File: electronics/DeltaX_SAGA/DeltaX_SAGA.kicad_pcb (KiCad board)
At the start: 4 copper layers, 50 x 50 mm, 73 parts, among them J1 USB_B_Micro, J10 M3_Encoder, J11 M12, J12 M21, J13 M22, J14 M31, J15 M33, J16 Thrower+, J17 Thrower-, J2 Programmer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

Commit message: PCB design updated
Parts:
- J11: value M12 -> OUT-
- J12: value M21 -> OUT+
- J13: value M22 -> OUT-
- J14: value M31 -> OUT+
- J15: value M33 -> OUT-
- J16: value Thrower+ -> THRWR+
- J17: value Thrower- -> THRWR-
- J4: value M11 -> OUT+
- J5: value Battery+ -> BAT+
- J7: value Battery- -> BAT-
- moved J4 0.58 mm to (135.8, 85.2)
- moved J16 0.50 mm to (172.4, 102.3)
- moved J17 0.50 mm to (172.4, 99.0)
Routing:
- net +3.3V: track 16.3 -> 16.7 mm, vias 11 -> 10
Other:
- board text added: "+"
- board text added: "-"
- board text added: "S"

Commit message: PCB dsign updated
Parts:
- moved Q1 4.78 mm to (164.0, 98.7)
- moved R3 4.34 mm to (158.7, 100.2), turned to 180 degrees
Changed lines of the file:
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@@
   )
   (footprint "Resistor_SMD:R_0603_1608Metric" (layer "B.Cu")
-    (at 154.3304 99.8728 90)
+    (at 158.66 100.15 180)
     (descr "Resistor SMD 0603 (1608 Metric), square (rectangular) end terminal, IPC_7351 nominal, (Body size source: IPC-SM-782 page 72, https://www.pcb-3d.com/wordpress/wp-content/uploads/ipc-sm-782a_amendment_1_and_2.pdf), generated with kicad-footprint-generator")
     (tags "resistor")
@@
     (property "Sheetname" "")
     (attr smd)
-    (fp_text reference "R3" (at -2.2972 -0.0704) (layer "B.SilkS")
-      (effects (font (size 1 1) (thickness 0.2)) (justify mirror))
-    )
-    (fp_text value "100" (at 0.9398 -1.1176 90) (layer "B.Fab")
+    (fp_text reference "R3" (at 0.91 1.46 180) (layer "B.SilkS")
+      (effects (font (size 1 1) (thickness 0.2)) (justify mirror))
+    )
+    (fp_text value "100" (at 0.9398 -1.1176) (layer "B.Fab")
       (effects (font (size 0.4 0.4) (thickness 0.1)) (justify mirror))
     )
-    (fp_text user "${REFERENCE}" (at 0 0 90) (layer "B.Fab")
+    (fp_text user "${REFERENCE}" (at 0 0) (layer "B.Fab")
       (effects (font (size 0.4 0.4) (thickness 0.06)) (justify mirror))
     )
@@
     (fp_line (start -0.8 0.4125) (end 0.8 0.4125) (layer "B.Fab") (width 0.1))
     (fp_line (start -0.8 -0.4125) (end -0.8 0.4125) (layer "B.Fab") (width 0.1))
-    (pad "1" smd roundrect (at -0.825 0 90) (size 0.8 0.95) (layers "B.Cu" "B.Paste" "B.Mask") (roundrect_rratio 0.25)
+    (pad "1" smd roundrect (at -0.825 0 180) (size 0.8 0.95) (layers "B.Cu" "B.Paste" "B.Mask") (roundrect_rratio 0.25)
       (net 83 "Net-(Q1-Pad4)") (pintype "passive"))
-    (pad "2" smd roundrect (at 0.825 0 90) (size 0.8 0.95) (layers "B.Cu" "B.Paste" "B.Mask") (roundrect_rratio 0.25)
+    (pad "2" smd roundrect (at 0.825 0 180) (size 0.8 0.95) (layers "B.Cu" "B.Paste" "B.Mask") (roundrect_rratio 0.25)
       (net 5 "GND2") (pintype "passive"))
     (model "${KICAD6_3DMODEL_DIR}/Resistor_SMD.3dshapes/R_0603_1608Metric.wrl"
@@
   )
   (footprint "BUK6Y10:TO127P600X120-5N" (layer "B.Cu")
-    (at 159.2114 99.21745 90)
+    (at 163.9664 98.72645 90)
     (property "MANUFACTURER" "")
     (property "MAXIMUM_PACKAGE_HEIGHT" "")
@@
   (segment (start 145.923 115.5192) (end 150.612695 115.5192) (width 0.25) (layer "B.Cu") (net 3))
   (segment (start 154.219495 119.126) (end 154.6606 119.126) (width 0.25) (layer "B.Cu") (net 3))
-  (via (at 158.5214 99.3902) (size 0.45) (drill 0.2) (layers "F.Cu" "B.Cu") (net 4))
-  (via (at 161.9504 97.9678) (size 0.45) (drill 0.2) (layers "F.Cu" "B.Cu") (net 4))
-  (via (at 160.0962 100.711) (size 0.45) (drill 0.2) (layers "F.Cu" "B.Cu") (net 4))
-  (via (at 158.496 100.711) (size 0.45) (drill 0.2) (layers "F.Cu" "B.Cu") (net 4))
-  (via (at 158.5214 97.9678) (size 0.45) (drill 0.2) (layers "F.Cu" "B.Cu") (net 4))
-  (via (at 161.9504 99.3902) (size 0.45) (drill 0.2) (layers "F.Cu" "B.Cu") (net 4))
-  (via (at 161.925 100.711) (size 0.45) (drill 0.2) (layers "F.Cu" "B.Cu") (net 4))
-  (via (at 160.1216 97.9678) (size 0.45) (drill 0.2) (layers "F.Cu" "B.Cu") (net 4))
-  (via (at 160.1216 99.3902) (size 0.45) (drill 0.2) (layers "F.Cu" "B.Cu") (net 4))
-  (via (at 161.9504 96.6724) (size 0.45) (drill 0.2) (layers "F.Cu" "B.Cu") (net 4))
-  (via (at 158.5214 96.6724) (size 0.45) (drill 0.2) (layers "F.Cu" "B.Cu") (net 4))
-  (via (at 160.1216 96.6724) (size 0.45) (drill 0.2) (layers "F.Cu" "B.Cu") (net 4))
+  (via (at 163.2764 98.8992) (size 0.45) (drill 0.2) (layers "F.Cu" "B.Cu") (net 4))
+  (via (at 166.7054 97.4768) (size 0.45) (drill 0.2) (layers "F.Cu" "B.Cu") (net 4))
+  (via (at 164.8512 100.22) (size 0.45) (drill 0.2) (layers "F.Cu" "B.Cu") (net 4))
+  (via (at 163.251 100.22) (size 0.45) (drill 0.2) (layers "F.Cu" "B.Cu") (net 4))
+  (via (at 163.2764 97.4768) (size 0.45) (drill 0.2) (layers "F.Cu" "B.Cu") (net 4))
+  (via (at 166.7054 98.8992) (size 0.45) (drill 0.2) (layers "F.Cu" "B.Cu") (net 4))
+  (via (at 166.68 100.22) (size 0.45) (drill 0.2) (layers "F.Cu" "B.Cu") (net 4))
+  (via (at 164.8766 97.4768) (size 0.45) (drill 0.2) (layers "F.Cu" "B.Cu") (net 4))
+  (via (at 164.8766 98.8992) (size 0.45) (drill 0.2) (layers "F.Cu" "B.Cu") (net 4))
+  (via (at 166.7054 96.1814) (size 0.45) (drill 0.2) (layers "F.Cu" "B.Cu") (net 4))
+  (via (at 163.2764 96.1814) (size 0.45) (drill 0.2) (layers "F.Cu" "B.Cu") (net 4))
+  (via (at 164.8766 96.1814) (size 0.45) (drill 0.2) (layers "F.Cu" "B.Cu") (net 4))
   (segment (start 138.2776 92.075) (end 138.596401 92.393801) (width 0.25) (layer "F.Cu") (net 5))
   (segment (start 134.734 104.5334) (end 134.9248 104.7242) (width 0.25) (layer "F.Cu") (net 5))
@@
   (via (at 172.4146 100.0086) (size 0.45) (drill 0.2) (layers "F.Cu" "B.Cu") (net 5))
   (via (at 138.2454 95.1) (size 0.45) (drill 0.2) (layers "F.Cu" "B.Cu") (net 5))
-  (via (at 154.051 98.8822) (size 0.45) (drill 0.2) (layers "F.Cu" "B.Cu") (net 5))
+  (via (at 157.62 100.42) (size 0.45) (drill 0.2) (layers "F.Cu" "B.Cu") (net 5))
   (via (at 172.339 95.4278) (size 0.45) (drill 0.2) (layers "F.Cu" "B.Cu") (net 5))
   (via (at 147.701 103.7082) (size 0.45) (drill 0.2) (layers "F.Cu" "B.Cu") (net 5))
@@
   (segment (start 162.1876 120.3008) (end 162.3516 120.1368) (width 0.153162) (layer "F.Cu") (net 7))
   (segment (start 167.061 120.1368) (end 170.7694 120.1368) (width 0.153162) (layer "F.Cu") (net 7))
-  (segment (start 165.8862 119.7368) (end 166.4868 119.1362) (width 0.153162) (layer "F.Cu") (net 8))
-  (segment (start 171.6706 119.634) (end 170.8682 119.634) (width 0.153162) (layer "F.Cu") (net 8))
-  (segment (start 162.358 119.7368) (end 165.8862 119.7368) (width 0.153162) (layer "F.Cu") (net 8))
-  (segment (start 162.122 119.5008) (end 162.358 119.7368) (width 0.153162) (layer "F.Cu") (net 8))
+  (segment (start 170.8682 119.634) (end 171.6706 119.634) (width 0.153162) (layer "F.Cu") (net 8))
+  (segment (start 162.404838 119.783638) (end 165.839362 119.783638) (width 0.153162) (layer "F.Cu") (net 8))
+  (segment (start 167.129238 119.783638) (end 170.718562 119.783638) (width 0.153162) (layer "F.Cu") (net 8))
+  (segment (start 161.1266 119.5008) (end 162.122 119.5008) (width 0.153162) (layer "F.Cu") (net 8))
+  (segment (start 170.718562 119.783638) (end 170.8682 119.634) (width 0.153162) (layer "F.Cu") (net 8))
+  (segment (start 162.122 119.5008) (end 162.404838 119.783638) (width 0.153162) (layer "F.Cu") (net 8))
+  (segment (start 165.839362 119.783638) (end 166.4868 119.1362) (width 0.153162) (layer "F.Cu") (net 8))
   (segment (start 166.4868 119.1362) (end 166.4868 118.6368) (width 0.153162) (layer "F.Cu") (net 8))
-  (segment (start 167.0824 119.7368) (end 170.7654 119.7368) (width 0.153162) (layer "F.Cu") (net 8))
-  (segment (start 170.8682 119.634) (end 170.7654 119.7368) (width 0.153162) (layer "F.Cu") (net 8))
-  (segment (start 166.4868 119.1412) (end 167.0824 119.7368) (width 0.153162) (layer "F.Cu") (net 8))
-  (segment (start 161.1266 119.5008) (end 162.122 119.5008) (width 0.153162) (layer "F.Cu") (net 8))
+  (segment (start 166.4868 119.1412) (end 167.129238 119.783638) (width 0.153162) (layer "F.Cu") (net 8))
   (segment (start 159.7466 116.5208) (end 159.7466 116.0212) (width 0.25) (layer "F.Cu") (net 10))
   (segment (start 148.4884 111.06) (end 148.4884 111.76) (width 0.25) (layer "F.Cu") (net 10))
@@
   (via (at 163.3982 90.75) (size 0.45) (drill 0.2) (layers "F.Cu" "B.Cu") (net 82))
   (via (at 138.8872 90.9828) (size 0.45) (drill 0.2) (layers "F.Cu" "B.Cu") (net 82))
-  (segment (start 154.41375 100.61445) (end 154.3304 100.6978) (width 0.25) (layer "B.Cu") (net 83))
-  (segment (start 156.5614 100.61445) (end 154.41375 100.61445) (width 0.25) (layer "B.Cu") (net 83))
+  (segment (start 161.3164 100.12345) (end 159.51155 100.12345) (width 0.25) (layer "B.Cu") (net 83))
+  (segment (start 159.51155 100.12345) (end 159.485 100.15) (width 0.25) (layer "B.Cu") (net 83))
   (segment (start 162.9664 123.9266) (end 162.9918 123.9012) (width 0.5) (layer "F.Cu") (net 84))
   (segment (start 140.7384 115.5192) (end 139.6492 115.5192) (width 0.25) (layer "F.Cu") (net 84))

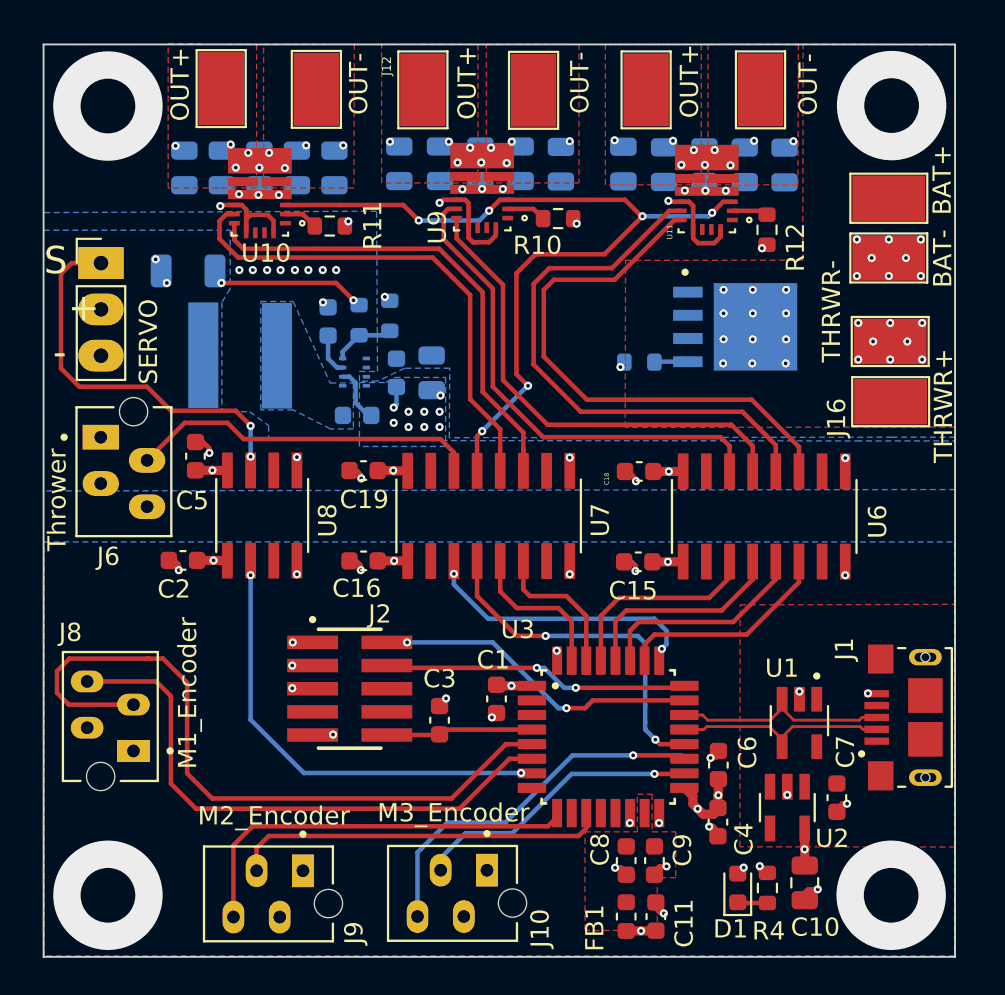
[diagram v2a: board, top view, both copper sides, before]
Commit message: PCB labels updated
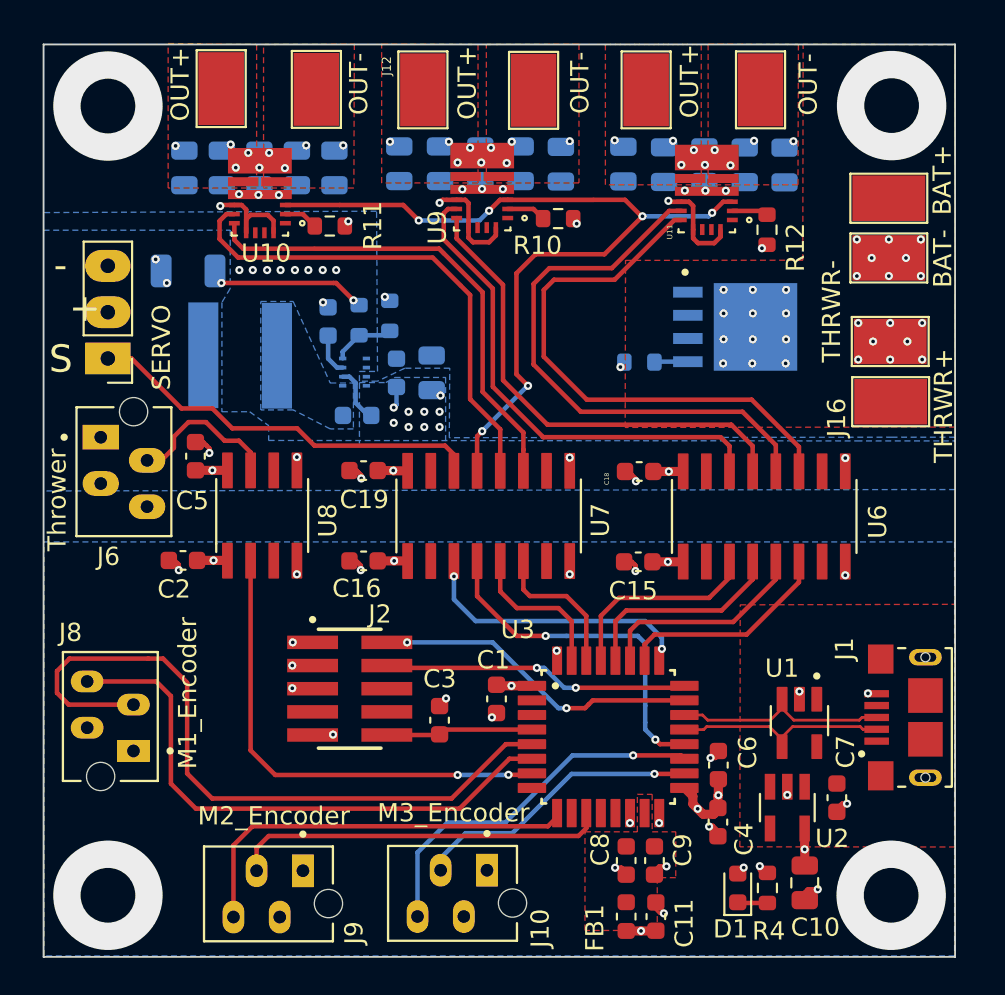
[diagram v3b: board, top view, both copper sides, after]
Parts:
- moved J3 5.25 mm to (129.5, 100.0), turned to 180 degrees
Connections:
- U3 pad 25: /Thrower_PWM -> /Servo_PWM
- U3 pad 7: /Servo_PWM -> /Thrower_PWM
- U7 pad 14: /Thrower_PWM_Isolated -> /Servo_PWM_Isolated
- U7 pad 3: /Thrower_PWM -> /Servo_PWM
- U8 pad 2: /Servo_PWM -> /Thrower_PWM
- U8 pad 7: /Servo_PWM_Isolated -> /Thrower_PWM_Isolated
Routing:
- net /Thrower_PWM_Isolated: track 19.4 -> 8.58 mm
- net /Thrower_PWM: track 15.8 -> 26.4 mm
- net /Servo_PWM: track 25.4 -> 15.7 mm
- net /Servo_PWM_Isolated: track 21.8 -> 22.1 mm, vias 2 -> 0

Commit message: PCB design with label optimised and updated
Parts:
- J16: value THRWR+ -> +
- J17: value THRWR- -> -
- J5: value BAT+ -> +
- J7: value BAT- -> -
- moved J16 0.20 mm to (172.2, 102.3)
- moved J17 0.20 mm to (172.2, 99.0)
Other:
- board text added: "BATTERY"
- board text added: "THROWER"
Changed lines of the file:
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@@
   )
   (footprint "1pinSMD:1PinSMD" (layer "F.Cu")
-    (at 172.3892 102.3454 180)
+    (at 172.1892 102.3454 180)
     (property "Sheetfile" "DeltaX_SAGA.kicad_sch")
     (property "Sheetname" "")
     (attr smd)
-    (fp_text reference "J16" (at 2.9082 -0.846 90 unlocked) (layer "F.SilkS")
+    (fp_text reference "J16" (at -0.2608 -2.3446 unlocked) (layer "F.Fab")
       (effects (font (size 1 1) (thickness 0.2)))
     )
-    (fp_text value "THRWR+" (at -2.9508 -0.1946 90 unlocked) (layer "F.SilkS")
-      (effects (font (size 1 1) (thickness 0.2)))
+    (fp_text value "+" (at -2.8808 0.0154 90 unlocked) (layer "F.SilkS")
+      (effects (font (size 1.5 1.5) (thickness 0.2)))
     )
     (fp_line (start 2.0574 1.3716) (end 2.0574 -1.3208) (layer "F.SilkS") (width 0.12))
@@
   )
   (footprint "1pinSMD:1PinSMD" (layer "F.Cu")
-    (at 172.3638 99.0434 180)
+    (at 172.1638 99.0434 180)
     (property "Sheetfile" "DeltaX_SAGA.kicad_sch")
     (property "Sheetname" "")
@@
       (effects (font (size 1 1) (thickness 0.2)))
     )
-    (fp_text value "THRWR-" (at 3.1638 1.6834 90 unlocked) (layer "F.SilkS")
-      (effects (font (size 1 1) (thickness 0.2)))
+    (fp_text value "-" (at -3.0062 -0.1866 180 unlocked) (layer "F.SilkS")
+      (effects (font (size 1.5 1.5) (thickness 0.2)))
     )
     (fp_line (start 2.0574 -1.3208) (end -2.159 -1.3208) (layer "F.SilkS") (width 0.12))
@@
     (property "Sheetname" "")
     (attr smd)
-    (fp_text reference "J7" (at -2.9298 -0.9918 90 unlocked) (layer "F.Fab")
+    (fp_text reference "J7" (at 1.5702 2.4582 90 unlocked) (layer "F.Fab")
       (effects (font (size 1 1) (thickness 0.2)))
     )
-    (fp_text value "BAT-" (at 2.9102 0.0582 90 unlocked) (layer "F.SilkS")
-      (effects (font (size 1 1) (thickness 0.2)))
+    (fp_text value "-" (at 2.8402 0.1482 180 unlocked) (layer "F.SilkS")
+      (effects (font (size 1.5 1.5) (thickness 0.2)))
     )
     (fp_line (start 2.0574 -1.3208) (end -2.159 -1.3208) (layer "F.SilkS") (width 0.12))
@@
     (property "Sheetname" "")
     (attr smd)
-    (fp_text reference "J5" (at -2.8998 -1.6252 90 unlocked) (layer "F.Fab")
+    (fp_text reference "J5" (at -1.4798 -2.2452 90 unlocked) (layer "F.Fab")
       (effects (font (size 1 1) (thickness 0.2)))
     )
-    (fp_text value "BAT+" (at 2.8802 -0.9752 90 unlocked) (layer "F.SilkS")
-      (effects (font (size 1 1) (thickness 0.2)))
+    (fp_text value "+" (at 2.7302 -0.0052 90 unlocked) (layer "F.SilkS")
+      (effects (font (size 1.5 1.5) (thickness 0.2)))
     )
     (fp_line (start 2.0574 -1.3208) (end -2.159 -1.3208) (layer "F.SilkS") (width 0.12))
@@
     (property "Sheetname" "")
     (attr through_hole)
-    (fp_text reference "Q1" (at -2.97255 2.7086) (layer "B.SilkS")
+    (fp_text reference "Q1" (at -3.15355 -2.7664) (layer "B.SilkS")
       (effects (font (size 1 1) (thickness 0.2)))
     )
@@
     (effects (font (size 1.5 1.5) (thickness 0.2)))
   )
+  (gr_text "BATTERY" (at 169.22 92.62 90) (layer "F.SilkS")
+    (effects (font (size 1 1) (thickness 0.2)))
+  )
+  (gr_text "THROWER" (at 168.9 100.41 90) (layer "F.SilkS")
+    (effects (font (size 1 1) (thickness 0.2)))
+  )
   (via (at 172.4914 86.0806) (size 6) (drill 3) (layers "F.Cu" "B.Cu") (free) (net 0))
   (via (at 129.5146 129.3876) (size 6) (drill 3) (layers "F.Cu" "B.Cu") (free) (net 0))
@@
   (via (at 139.7694 95.1) (size 0.45) (drill 0.2) (layers "F.Cu" "B.Cu") (net 5))
   (via (at 158.4706 106.68) (size 0.45) (drill 0.2) (layers "F.Cu" "B.Cu") (net 5))
-  (via (at 174.1672 98.002) (size 0.45) (drill 0.2) (layers "F.Cu" "B.Cu") (net 5))
+  (via (at 173.9672 98.002) (size 0.45) (drill 0.2) (layers "F.Cu" "B.Cu") (net 5))
   (via (at 148.209 88.0618) (size 0.45) (drill 0.2) (layers "F.Cu" "B.Cu") (net 5))
   (via (at 147.701 91.4146) (size 0.45) (drill 0.2) (layers "F.Cu" "B.Cu") (net 5))
@@
   (via (at 167.1066 88.0364) (size 0.45) (drill 0.2) (layers "F.Cu" "B.Cu") (net 5))
   (via (at 142.6972 92.4306) (size 0.45) (drill 0.2) (layers "F.Cu" "B.Cu") (net 5))
-  (via (at 173.3544 99.018) (size 0.45) (drill 0.2) (layers "F.Cu" "B.Cu") (net 5))
+  (via (at 173.1544 99.018) (size 0.45) (drill 0.2) (layers "F.Cu" "B.Cu") (net 5))
   (via (at 137.458 95.1) (size 0.45) (drill 0.2) (layers "F.Cu" "B.Cu") (net 5))
   (via (at 174.0916 95.4278) (size 0.45) (drill 0.2) (layers "F.Cu" "B.Cu") (net 5))
@@
   (via (at 146.8628 103.7082) (size 0.45) (drill 0.2) (layers "F.Cu" "B.Cu") (net 5))
   (via (at 144.7 96.57) (size 0.45) (drill 0.2) (layers "F.Cu" "B.Cu") (net 5))
-  (via (at 170.662 98.002) (size 0.45) (drill 0.2) (layers "F.Cu" "B.Cu") (net 5))
+  (via (at 170.462 98.002) (size 0.45) (drill 0.2) (layers "F.Cu" "B.Cu") (net 5))
   (via (at 150.5204 88.392) (size 0.45) (drill 0.2) (layers "F.Cu" "B.Cu") (net 5))
   (via (at 133.223 88.2904) (size 0.45) (drill 0.2) (layers "F.Cu" "B.Cu") (net 5))
@@
   (via (at 142.4178 88.265) (size 0.45) (drill 0.2) (layers "F.Cu" "B.Cu") (net 5))
   (via (at 151.6634 88.0618) (size 0.45) (drill 0.2) (layers "F.Cu" "B.Cu") (net 5))
-  (via (at 170.662 100.0086) (size 0.45) (drill 0.2) (layers "F.Cu" "B.Cu") (net 5))
+  (via (at 170.462 100.0086) (size 0.45) (drill 0.2) (layers "F.Cu" "B.Cu") (net 5))
   (via (at 138.982 95.1) (size 0.45) (drill 0.2) (layers "F.Cu" "B.Cu") (net 5))
   (via (at 149.987 89.2048) (size 0.45) (drill 0.2) (layers "F.Cu" "B.Cu") (net 5))
   (via (at 137.8204 89.4842) (size 0.45) (drill 0.2) (layers "F.Cu" "B.Cu") (net 5))
-  (via (at 174.1672 100.0086) (size 0.45) (drill 0.2) (layers "F.Cu" "B.Cu") (net 5))
+  (via (at 173.9672 100.0086) (size 0.45) (drill 0.2) (layers "F.Cu" "B.Cu") (net 5))
   (via (at 144.9832 88.0618) (size 0.45) (drill 0.2) (layers "F.Cu" "B.Cu") (net 5))
   (via (at 143.4084 106.5276) (size 0.45) (drill 0.2) (layers "F.Cu" "B.Cu") (net 5))
@@
   (via (at 170.5864 95.4278) (size 0.45) (drill 0.2) (layers "F.Cu" "B.Cu") (net 5))
   (via (at 165.3794 93.9038) (size 0.45) (drill 0.2) (layers "F.Cu" "B.Cu") (net 5))
-  (via (at 172.4146 100.0086) (size 0.45) (drill 0.2) (layers "F.Cu" "B.Cu") (net 5))
+  (via (at 172.2146 100.0086) (size 0.45) (drill 0.2) (layers "F.Cu" "B.Cu") (net 5))
   (via (at 138.2454 95.1) (size 0.45) (drill 0.2) (layers "F.Cu" "B.Cu") (net 5))
   (via (at 157.62 100.42) (size 0.45) (drill 0.2) (layers "F.Cu" "B.Cu") (net 5))
@@
   (via (at 171.3992 94.4372) (size 0.45) (drill 0.2) (layers "F.Cu" "B.Cu") (net 5))
   (via (at 160.9598 89.3318) (size 0.45) (drill 0.2) (layers "F.Cu" "B.Cu") (net 5))
-  (via (at 171.4748 99.018) (size 0.45) (drill 0.2) (layers "F.Cu" "B.Cu") (net 5))
+  (via (at 171.2748 99.018) (size 0.45) (drill 0.2) (layers "F.Cu" "B.Cu") (net 5))
   (via (at 140.506 95.1) (size 0.45) (drill 0.2) (layers "F.Cu" "B.Cu") (net 5))
   (via (at 135.675224 91.590646) (size 0.45) (drill 0.2) (layers "F.Cu" "B.Cu") (net 5))
@@
   (via (at 148.6916 89.2048) (size 0.45) (drill 0.2) (layers "F.Cu" "B.Cu") (net 5))
   (via (at 137.2108 88.6714) (size 0.45) (drill 0.2) (layers "F.Cu" "B.Cu") (net 5))
-  (via (at 172.4146 98.002) (size 0.45) (drill 0.2) (layers "F.Cu" "B.Cu") (net 5))
+  (via (at 172.2146 98.002) (size 0.45) (drill 0.2) (layers "F.Cu" "B.Cu") (net 5))
   (via (at 147.7518 101.981) (size 0.45) (drill 0.2) (layers "F.Cu" "B.Cu") (net 5))
   (segment (start 166.624 88.3056) (end 166.8374 88.3056) (width 0.25) (layer "B.Cu") (net 5))
